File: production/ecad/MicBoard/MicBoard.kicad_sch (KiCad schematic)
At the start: 14 parts, among them U2 OPA330xxDCK

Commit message: kaden told me to commit
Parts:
- removed MK1: Microphone, symbol Device:Microphone
- removed U2: OPA330xxDCK, symbol Amplifier_Operational:OPA330xxDCK
- added U3: CMA-4544PF-W, CMA_CUI_9P7X9P7_CUD, symbol 2024-02-15_23-42-42:CMA-4544PF-W
- added U4: OPA1671IDBVR, SOT23-DBV5_TEX, symbol 2024-02-15_23-46-41:OPA1671IDBVR
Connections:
- net +3.3V: now also U4.5 (V+)
- net GND: now also U3.1, U4.2 (V-)
- net at C4.1, R4.2: now also U3.2
- net at C4.2, R3.2, R5.1: now also U4.3 (+IN)
- net at C1.1, R1.1, R2.2: now also U4.4 (-IN)
- net at C1.2, C3.1, R2.1: now also U4.1 (OUT)
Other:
- moved on the sheet: C1, C3, R2, U1

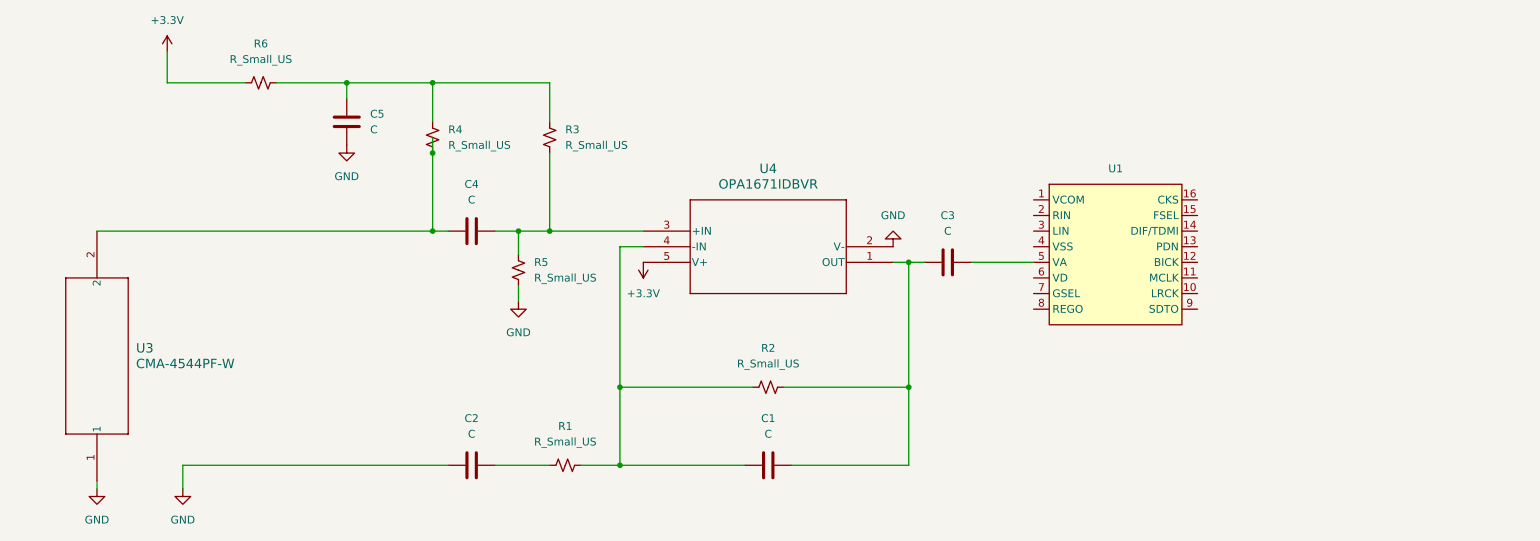
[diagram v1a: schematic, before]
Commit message: added connectors
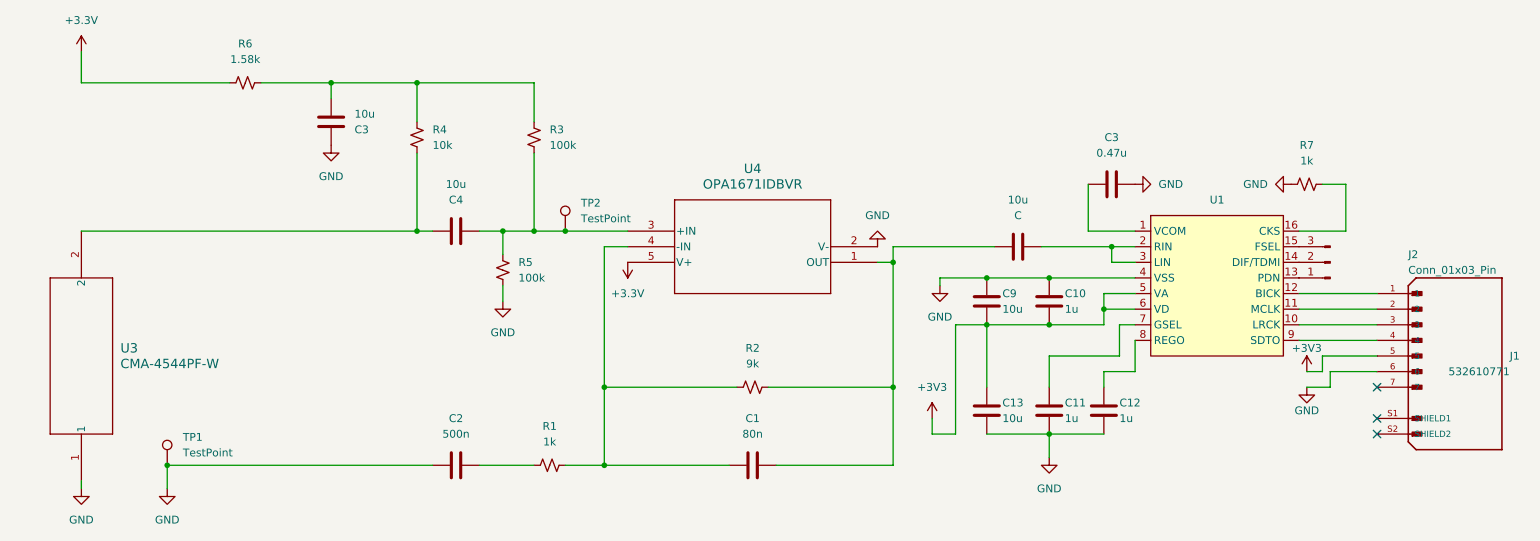
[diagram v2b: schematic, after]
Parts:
- added C10, C11, C12: 1u, symbol Device:C
- added C13, C9: 10u, symbol Device:C
- added C3: 0.47u, symbol Device:C
- added J1: 532610771, 532610771:MOLEX_532610771, symbol 532610771:532610771
- added J2: Conn_01x03_Pin, symbol Connector:Conn_01x03_Pin
- added R7: 1k, symbol Device:R_Small_US
- added TP1, TP2: TestPoint, symbol Connector:TestPoint
- 10u: renamed from C5; value C -> C3
- 10u: renamed from C4; value C -> C4
- C1: value C -> 80n
- C2: value C -> 500n
- R1: value R_Small_US -> 1k
- R2: value R_Small_US -> 9k
- R3, R5: value R_Small_US -> 100k
- R4: value R_Small_US -> 10k
- R6: value R_Small_US -> 1.58k
- renumbered C3 to 10u
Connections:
- net GND: now also U1.4 (VSS), C10.1, C11.2, C12.2, C13.2, C3.2, C9.1, J1.6, R7.1, TP1.1
- net at 10u.2, R3.2, R5.1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: now also TP2.1
- net at 10u.2: now also U1.2 (RIN), U1.3 (LIN); no longer U1.5 (VA)
- net at U1.1 (VCOM): now also C3.1
- net at U1.10 (LRCK): now also J1.3
- net at U1.11 (MCLK): now also J1.2
- net at U1.12 (BICK): now also J1.1
- net at U1.13 (PDN): now also J2.1 (Pin_1)
- net at U1.14 (DIF/TDMI): now also J2.2 (Pin_2)
- net at U1.15 (FSEL): now also J2.3 (Pin_3)
- net at U1.16 (CKS): now also R7.2
- net +3V3: now reaches U1.6 (VD)
- net +3V3: now also U1.5 (VA), C10.2, C13.1, C9.2, J1.5
- net at U1.7 (GSEL): now also C11.1
- net at U1.8 (REGO): now also C12.1
- net at U1.9 (SDTO): now also J1.4
- no-connect marks 0 -> 3
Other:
- moved on the sheet: 10u, C1, C2, R1, R2, R3, R4, R5, R6, U1, U3, U4

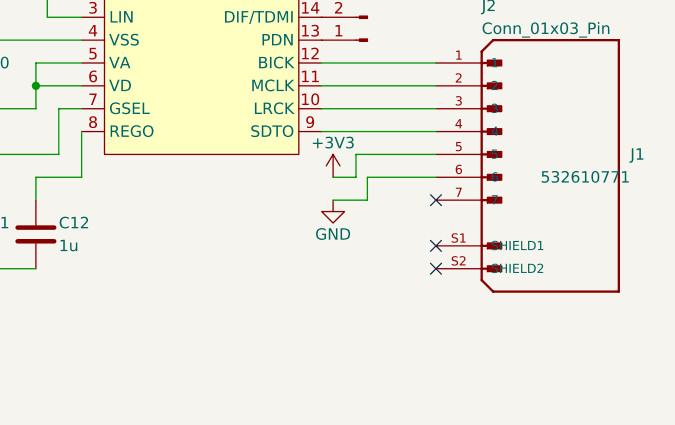
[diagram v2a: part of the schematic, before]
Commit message: add ground shields and extra connector
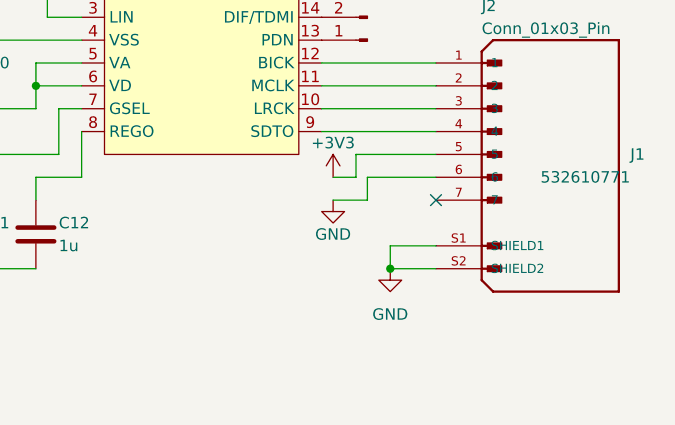
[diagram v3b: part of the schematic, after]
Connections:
- net GND: now also J1.S1 (SHIELD1), J1.S2 (SHIELD2)
- no-connect marks 3 -> 1
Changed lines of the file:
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@@
 (kicad_sch (version 20230121) (generator eeschema)
   (paper "A4")
+  (junction (at 242.57 119.38) (diameter 0) (color 0 0 0 0)
+  )
   (junction (at 203.2 99.06) (diameter 0) (color 0 0 0 0)
   )
@@
   (junction (at 194.31 93.98) (diameter 0) (color 0 0 0 0)
   )
-  (no_connect (at 247.65 116.84))
-  (no_connect (at 247.65 119.38))
   (no_connect (at 247.65 111.76))
   (wire (pts (xy 194.31 93.98) (xy 208.28 93.98))
@@
     (stroke (width 0) (type default))
   )
+  (wire (pts (xy 247.65 116.84) (xy 242.57 116.84))
+    (stroke (width 0) (type default))
+  )
   (wire (pts (xy 184.15 101.6) (xy 184.15 111.76))
     (stroke (width 0) (type default))
@@
     (stroke (width 0) (type default))
   )
+  (wire (pts (xy 242.57 119.38) (xy 247.65 119.38))
+    (stroke (width 0) (type default))
+  )
   (wire (pts (xy 115.57 124.46) (xy 121.92 124.46))
     (stroke (width 0) (type default))
@@
   )
   (wire (pts (xy 208.28 104.14) (xy 208.28 109.22))
+    (stroke (width 0) (type default))
+  )
+  (wire (pts (xy 242.57 116.84) (xy 242.57 119.38))
     (stroke (width 0) (type default))
   )
@@
         )
       )
+    )
+  )
+  (symbol (lib_id "power:GND") (at 242.57 119.38 0) (unit 1)
+    (in_bom yes) (on_board yes) (dnp no) (fields_autoplaced)
+    (property "Reference" "#PWR05" (at 242.57 125.73 0)
+      (effects (font (size 1.27 1.27)) hide)
+    )
+    (property "Value" "GND" (at 242.57 124.46 0)
+      (effects (font (size 1.27 1.27)))
+    )
+    (property "Footprint" "" (at 242.57 119.38 0)
+      (effects (font (size 1.27 1.27)) hide)
+    )
+    (property "Datasheet" "" (at 242.57 119.38 0)
+      (effects (font (size 1.27 1.27)) hide)
+    )
+    (pin "1")
+    (instances
+      (project "cstar-audio"
+        (path "/16a488a1-12e9-4eb7-bbd0-d500eeb9c89a"
+          (reference "#PWR05") (unit 1)
+        )
+      )
+      (project "MicBoard"
+        (path "/35817364-8fba-4697-86bd-839867f6fab6"
+          (reference "#PWR012") (unit 1)
+        )
+      )

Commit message: initial mic layout
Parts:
- removed U3: CMA-4544PF-W, CMA_CUI_9P7X9P7_CUD, symbol 2024-02-15_23-42-42:CMA-4544PF-W
- added MK1: CMA-4544PF-W, cstar_mic_footprints:MIC_CMA-4544PF-W, symbol CMA-4544PF-W:CMA-4544PF-W
- C1: renamed from 10u; value C3 -> 10u; footprint (none) -> Capacitor_SMD:C_0805_2012Metric
- C10: renamed from C12; footprint (none) -> Capacitor_SMD:C_0805_2012Metric
- C11: renamed from C3; footprint (none) -> Capacitor_SMD:C_0805_2012Metric
- C2: renamed from 10u; value C4 -> 10u; footprint (none) -> Capacitor_SMD:C_0805_2012Metric
- C3: renamed from C2; footprint (none) -> Capacitor_SMD:C_0805_2012Metric
- C4: renamed from C1; footprint (none) -> Capacitor_SMD:C_0805_2012Metric
- C5: renamed from C9; footprint (none) -> Capacitor_SMD:C_0805_2012Metric
- C6: renamed from C13; footprint (none) -> Capacitor_SMD:C_0805_2012Metric
- C7: renamed from 10u; value C -> 10u; footprint (none) -> Capacitor_SMD:C_0805_2012Metric
- C8: renamed from C10; footprint (none) -> Capacitor_SMD:C_0805_2012Metric
- C9: renamed from C11; footprint (none) -> Capacitor_SMD:C_0805_2012Metric
- J1: renamed from J2; footprint (none) -> Connector_PinHeader_2.54mm:PinHeader_1x03_P2.54mm_Vertical
- J2: renamed from J1; footprint 532610771:MOLEX_532610771 -> cstar_mic_footprints:MOLEX_532610771
- R1: renamed from R6; footprint (none) -> Resistor_SMD:R_0805_2012Metric
- R2: renamed from R4; footprint (none) -> Resistor_SMD:R_0805_2012Metric
- R3: renamed from R5; footprint (none) -> Resistor_SMD:R_0805_2012Metric
- R4: renamed from R3; footprint (none) -> Resistor_SMD:R_0805_2012Metric
- R5: renamed from R1; footprint (none) -> Resistor_SMD:R_0805_2012Metric
- R6: renamed from R2; footprint (none) -> Resistor_SMD:R_0805_2012Metric
- R7: footprint (none) -> Resistor_SMD:R_0805_2012Metric
- TP1, TP2: footprint (none) -> TestPoint:TestPoint_Pad_D1.0mm
- U2: renamed from U4; footprint SOT23-DBV5_TEX -> cstar_mic_footprints:SOT23-DBV5_TEX-L
- U3: renamed from U1; footprint (none) -> cstar_mic_footprints:SOIC_AK5720_AKM-L; symbol AK5720VT:AK5720VT -> ADC:AK5720VT
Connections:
- net GND: now also MK1.2
- net at C2.1, R2.2: now also MK1.1
- net at J2.1: now also U3.9 (SDTO); no longer U3.12 (BICK)
- net at J2.2: now also U3.10 (LRCK); no longer U3.11 (MCLK)
- net at J2.3: now also U3.11 (MCLK); no longer U3.10 (LRCK)
- net at J2.4: now also U3.12 (BICK); no longer U3.9 (SDTO)
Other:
- moved on the sheet: C1, C10, C11, C2, C3, C4, C5, C6, C7, C8, C9, R1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

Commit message: fix drc errors
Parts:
- added TP3: TestPoint, TestPoint:TestPoint_Pad_D1.0mm, symbol Connector:TestPoint
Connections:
- net +3.3V is gone; now on net +3V3: R1.2, U2.5 (V+)
- net at C4.2, C7.1, R6.1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: now also TP3.1
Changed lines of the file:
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@@
   (junction (at 144.78 111.76) (diameter 0) (color 0 0 0 0)
+  )
+  (junction (at 149.86 88.9) (diameter 0) (color 0 0 0 0)
   )
   (junction (at 91.44 86.36) (diameter 0) (color 0 0 0 0)
@@
     (stroke (width 0) (type default))
   )
-  (wire (pts (xy 144.78 88.9) (xy 161.29 88.9))
+  (wire (pts (xy 144.78 88.9) (xy 149.86 88.9))
     (stroke (width 0) (type default))
   )
@@
     (stroke (width 0) (type default))
   )
+  (wire (pts (xy 149.86 88.9) (xy 161.29 88.9))
+    (stroke (width 0) (type default))
+  )
   (wire (pts (xy 41.91 62.23) (xy 30.48 62.23))
     (stroke (width 0) (type default))
@@
         (path "/35817364-8fba-4697-86bd-839867f6fab6"
           (reference "C3") (unit 1)
+        )
+      )
+    )
+  )
+  (symbol (lib_id "power:+3V3") (at 30.48 57.15 0) (unit 1)
+    (in_bom yes) (on_board yes) (dnp no) (fields_autoplaced)
+    (property "Reference" "#PWR01" (at 30.48 60.96 0)
+      (effects (font (size 1.27 1.27)) hide)
+    )
+    (property "Value" "+3V3" (at 30.48 52.07 0)
+      (effects (font (size 1.27 1.27)))
+    )
+    (property "Footprint" "" (at 30.48 57.15 0)
+      (effects (font (size 1.27 1.27)) hide)
+    )
+    (property "Datasheet" "" (at 30.48 57.15 0)
+      (effects (font (size 1.27 1.27)) hide)
+    )
+    (pin "1")
+    (instances
+      (project "MicBoard"
+        (path "/35817364-8fba-4697-86bd-839867f6fab6"
+          (reference "#PWR01") (unit 1)
         )
       )
@@
     )
   )
+  (symbol (lib_id "Connector:TestPoint") (at 149.86 88.9 0) (unit 1)
+    (in_bom yes) (on_board yes) (dnp no) (fields_autoplaced)
+    (property "Reference" "TP3" (at 152.4 84.328 0)
+      (effects (font (size 1.27 1.27)) (justify left))
+    )
+    (property "Value" "TestPoint" (at 152.4 86.868 0)
+      (effects (font (size 1.27 1.27)) (justify left))
+    )
+    (property "Footprint" "TestPoint:TestPoint_Pad_D1.0mm" (at 154.94 88.9 0)
+      (effects (font (size 1.27 1.27)) hide)
+    )
+    (property "Datasheet" "~" (at 154.94 88.9 0)
+      (effects (font (size 1.27 1.27)) hide)
+    )
+    (pin "1")
+    (instances
+      (project "MicBoard"
+        (path "/35817364-8fba-4697-86bd-839867f6fab6"
+          (reference "TP3") (unit 1)
+        )
+      )
+    )
+  )
   (symbol (lib_id "Device:C") (at 165.1 88.9 90) (unit 1)
     (in_bom yes) (on_board yes) (dnp no) (fields_autoplaced)
@@
     )
   )
-  (symbol (lib_id "power:+3.3V") (at 105.41 99.06 0) (unit 1)
+  (symbol (lib_id "power:+3V3") (at 105.41 99.06 0) (unit 1)
     (in_bom yes) (on_board yes) (dnp no) (fields_autoplaced)
     (property "Reference" "#PWR06" (at 105.41 102.87 0)
       (effects (font (size 1.27 1.27)) hide)
     )
-    (property "Value" "+3.3V" (at 105.41 93.98 0)
+    (property "Value" "+3V3" (at 105.41 93.98 0)
       (effects (font (size 1.27 1.27)))
     )
@@
         )
       )
-    )
-  )
-  (symbol (lib_id "power:+3.3V") (at 30.48 57.15 0) (unit 1)
-    (in_bom yes) (on_board yes) (dnp no) (fields_autoplaced)
-    (property "Reference" "#PWR01" (at 30.48 60.96 0)
-      (effects (font (size 1.27 1.27)) hide)
-    )
-    (property "Value" "+3.3V" (at 30.48 52.07 0)
-      (effects (font (size 1.27 1.27)))
-    )
-    (property "Footprint" "" (at 30.48 57.15 0)
-      (effects (font (size 1.27 1.27)) hide)
-    )
-    (property "Datasheet" "" (at 30.48 57.15 0)
-      (effects (font (size 1.27 1.27)) hide)
-    )
-    (pin "1")
-    (instances
-      (project "MicBoard"
-        (path "/35817364-8fba-4697-86bd-839867f6fab6"
-          (reference "#PWR01") (unit 1)
-        )
-      )
